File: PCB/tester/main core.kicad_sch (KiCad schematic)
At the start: 44 parts, among them J2 Conn_02x03_Odd_Even, Q1 DMN63D8L-7, SW1 SW_SPST, SW2 SW_SPST, SW3 SW_SPST, SW4 SW_SPST, SW5 SW_SPST, SW6 SW_SPST, SW7 SW_SPST, SW8 SW_SPST, SW9 SW_SPST, U5 ATXMEGA32A4U-MH

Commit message: promenores componentes para a BOM
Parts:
- J2: value Conn_02x03_Odd_Even -> PR20203VBDN
- SW1, SW2, SW3, SW4, SW5, SW6, SW7, SW8, SW9: value SW_SPST -> TL3305BF260QG
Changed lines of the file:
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@@
 			)
 		)
-		(property "Value" "SW_SPST"
+		(property "Value" "TL3305BF260QG"
 			(at 22.86 146.05 0)
 			(hide yes)
@@
 			)
 		)
-		(property "Value" "SW_SPST"
+		(property "Value" "TL3305BF260QG"
 			(at 53.34 146.05 0)
 			(hide yes)
@@
 			)
 		)
-		(property "Value" "SW_SPST"
+		(property "Value" "TL3305BF260QG"
 			(at 52.07 121.92 0)
 			(hide yes)
@@
 			)
 		)
-		(property "Value" "SW_SPST"
+		(property "Value" "TL3305BF260QG"
 			(at 52.07 96.52 0)
 			(hide yes)
@@
 			)
 		)
-		(property "Value" "SW_SPST"
+		(property "Value" "TL3305BF260QG"
 			(at 24.13 48.26 0)
 			(hide yes)
@@
 			)
 		)
-		(property "Value" "SW_SPST"
+		(property "Value" "TL3305BF260QG"
 			(at 54.61 48.26 0)
 			(hide yes)
@@
 			)
 		)
-		(property "Value" "SW_SPST"
+		(property "Value" "TL3305BF260QG"
 			(at 22.86 121.92 0)
 			(hide yes)
@@
 			)
 		)
-		(property "Value" "Conn_02x03_Odd_Even"
+		(property "Value" "PR20203VBDN"
 			(at 189.23 133.35 0)
 			(hide yes)
@@
 			)
 		)
-		(property "Value" "SW_SPST"
+		(property "Value" "TL3305BF260QG"
 			(at 22.86 96.52 0)
 			(hide yes)
@@
 			)
 		)
-		(property "Value" "SW_SPST"
+		(property "Value" "TL3305BF260QG"
 			(at 25.4 15.24 0)
 			(hide yes)

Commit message: sync with main
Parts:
- R10, R11, R12, R16, R9: value 2k -> 330R; MPN ERJ-2RKF2001X -> CRCW0402330RFKEDHP; OEPSPN OEPS020007 -> OEPS020191

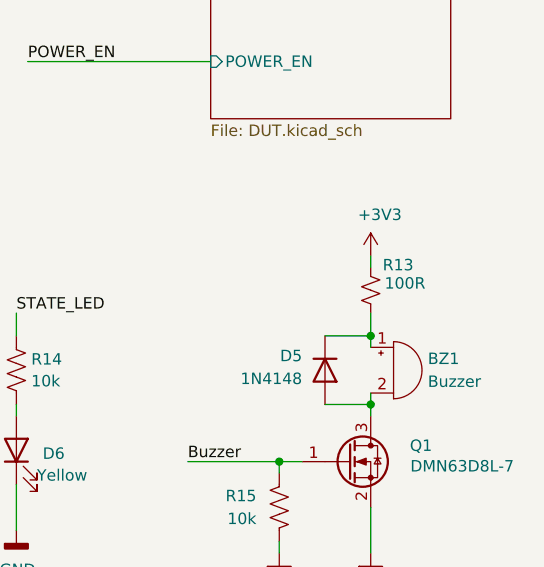
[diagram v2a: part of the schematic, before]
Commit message: início Rev.C
- corrigido pinout dos relais
- corrigido valor & MPN & OEPSPN de R13 =1R
- feito re-routing: DRC=0
- gerados ficheiros de produção
- BOM actualizada
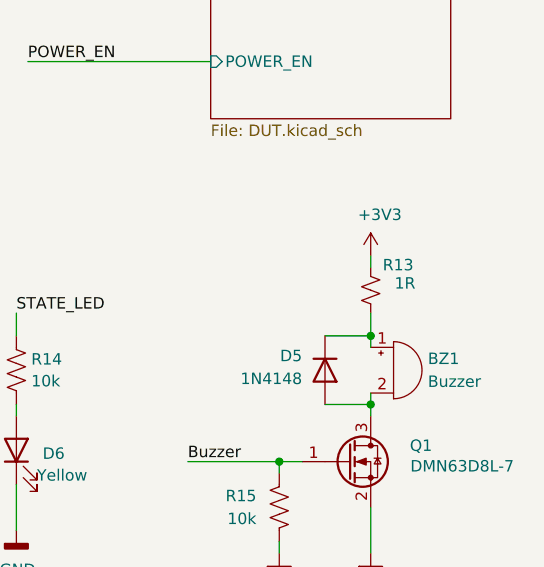
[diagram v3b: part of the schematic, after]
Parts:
- D5: MPN 1N4148WX-TP -> 1N4148WS-E3-18; OEPSPN OEPS030017 -> OEPS030052
- R13: value 100R -> 1R; MPN RCS0402100RFKED -> CRCW04021R00FKEDC; OEPSPN OEPS020028 -> OEPS020061
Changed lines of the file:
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@@
 			)
 		)
-		(property "OEPSPN" "OEPS030017"
+		(property "OEPSPN" "OEPS030052"
 			(at 254 143.51 90)
 			(hide yes)
@@
 			)
 		)
-		(property "MPN" "1N4148WX-TP"
+		(property "MPN" "1N4148WS-E3-18"
 			(at 254 143.51 90)
 			(hide yes)
@@
 			)
 		)
-		(property "Value" "100R"
+		(property "Value" "1R"
 			(at 262.89 133.858 0)
 			(show_name no)
@@
 			)
 		)
-		(property "Description" "RESISTOR:   SMD 0402 100Ω ±1% 0.250W   [RCS0402100RFKED] [SMD]"
+		(property "Description" "SMD 0402 1Ω ±1% 0.063W"
 			(at 259.08 134.62 0)
 			(hide yes)
@@
 			)
 		)
-		(property "MPN" "RCS0402100RFKED"
+		(property "MPN" "CRCW04021R00FKEDC"
 			(at 259.08 134.62 90)
 			(hide yes)
@@
 			)
 		)
-		(property "OEPSPN" "OEPS020028"
+		(property "OEPSPN" "OEPS020061"
 			(at 259.08 134.62 90)
 			(hide yes)
